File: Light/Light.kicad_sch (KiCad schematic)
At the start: 40 parts

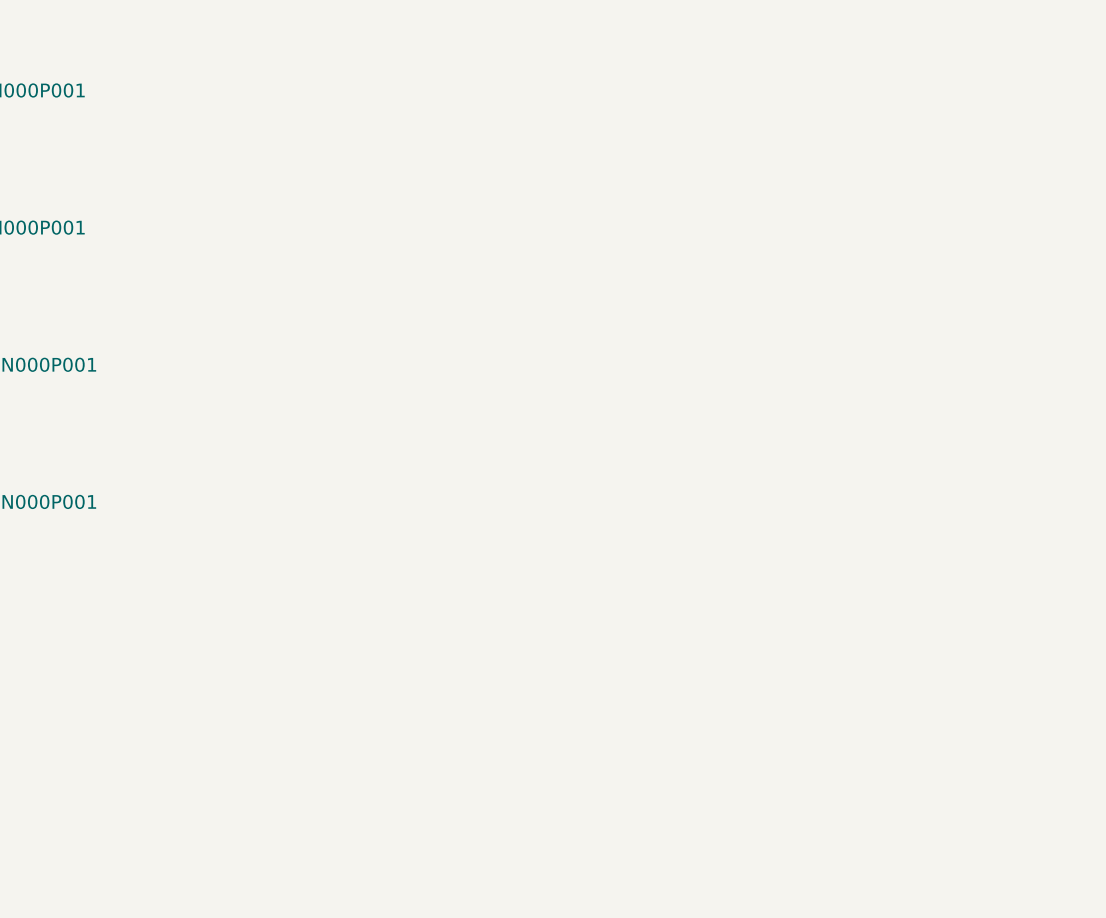
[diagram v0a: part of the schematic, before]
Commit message: added led brigthness calculations
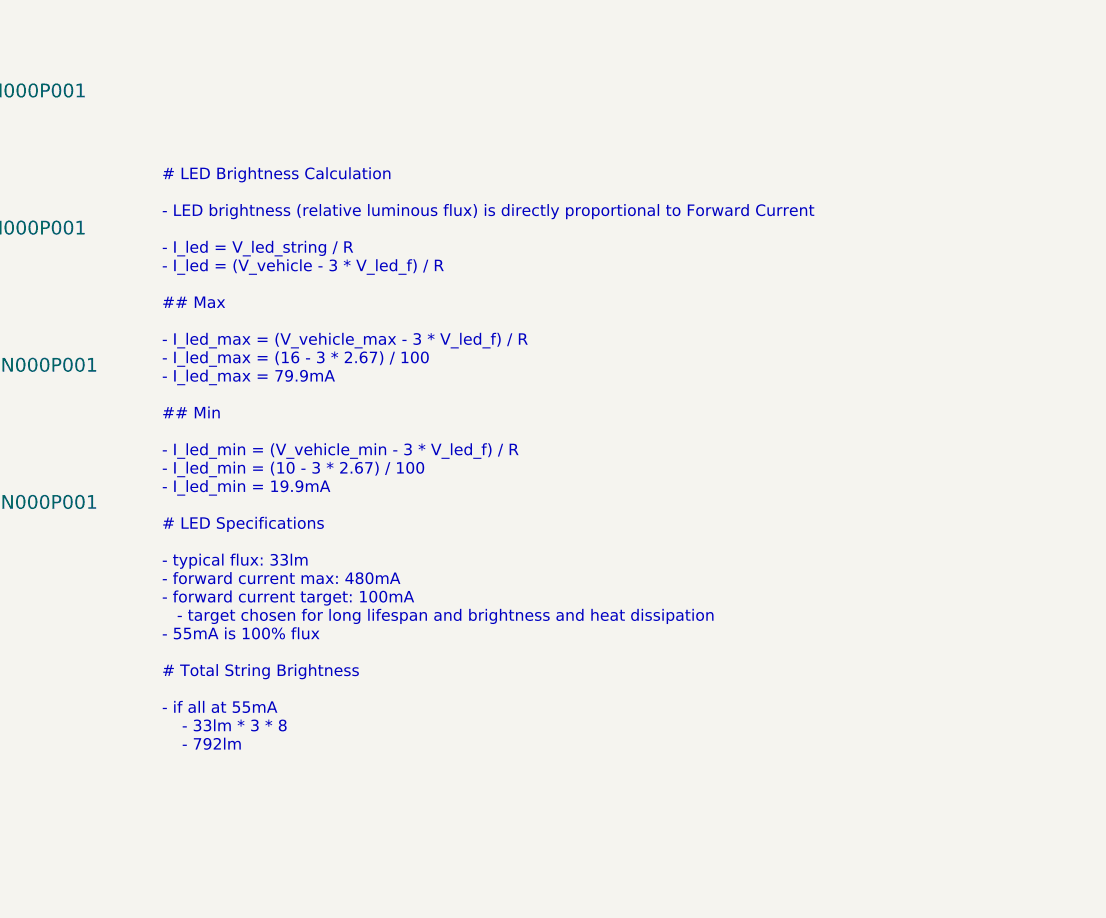
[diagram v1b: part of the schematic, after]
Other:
- note added: "# LED Brightness Calculation - LED brightness (relative luminous flux) is directly proportional to Forward Current - I_led = V_led_string / R - I_led = (V_vehicle - 3 * V_led_f) / R ## Max - I_led_max = (V_vehicle_max - 3 * V_led_f) / R - I_led_max = (16 - 3 * 2.67) / 100 - I_led_max = 79.9mA ## Min - I_led_min = (V_vehicle_min - 3 * V_led_f) / R - I_led_min = (10 - 3 * 2.67) / 100 - I_led_min = 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"
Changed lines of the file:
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@@
+		)
+	)
+	(text "# LED Brightness Calculation\n\n- LED brightness (relative luminous flux) is directly proportional to Forward Current\n\n- I_led = V_led_string / R\n- I_led = (V_vehicle - 3 * V_led_f) / R\n\n## Max\n\n- I_led_max = (V_vehicle_max - 3 * V_led_f) / R\n- I_led_max = (16 - 3 * 2.67) / 100\n- I_led_max = 79.9mA\n\n## Min\n\n- I_led_min = (V_vehicle_min - 3 * V_led_f) / R\n- I_led_min = (10 - 3 * 2.67) / 100\n- I_led_min = 19.9mA\n\n# LED Specifications\n\n- typical flux: 33lm\n- forward current max: 480mA\n- forward current target: 100mA\n   - target chosen for long lifespan and brightness and heat dissipation\n- 55mA is 100% flux\n\n# Total String Brightness\n\n- if all at 55mA\n    - 33lm * 3 * 8\n    - 792lm"
+		(exclude_from_sim no)
+		(at 195.58 122.428 0)
+		(effects
+			(font
+				(size 1.27 1.27)
+			)
+			(justify left)
 		)
 	)

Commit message: general placement and first pass at routing
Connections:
- net GND: now also LED15.1, LED18.1; no longer LED22.1, LED23.1
- net at R7.2: now also LED19.2; no longer LED15.2
- net at R6.2: now also LED16.2; no longer LED14.2
- net at LED21.2: now also LED20.1; no longer LED17.1
- net at R8.2: now also LED22.2; no longer LED16.2
- net at LED16.1: now also LED17.2; no longer LED20.2
- net at LED19.1: now also LED20.2; no longer LED23.2
- net at LED13.1: now also LED14.2; no longer LED17.2
- net at LED24.2: now also LED23.1; no longer LED20.1
- net at LED14.1: now also LED15.2; no longer LED18.2
- new net: LED17.1, LED18.2
- new net: LED22.1, LED23.2
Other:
- moved on the sheet: LED14, LED15, LED16, LED17, LED18, LED19, LED20, LED21, LED22, LED23
